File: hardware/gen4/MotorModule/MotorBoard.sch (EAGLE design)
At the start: 65 parts, among them IC1 XMEGA16A4A, IC2 3.3V REG, M1O1 TEST_PT, M1O2 TEST_PT, M1O3 TEST_PT

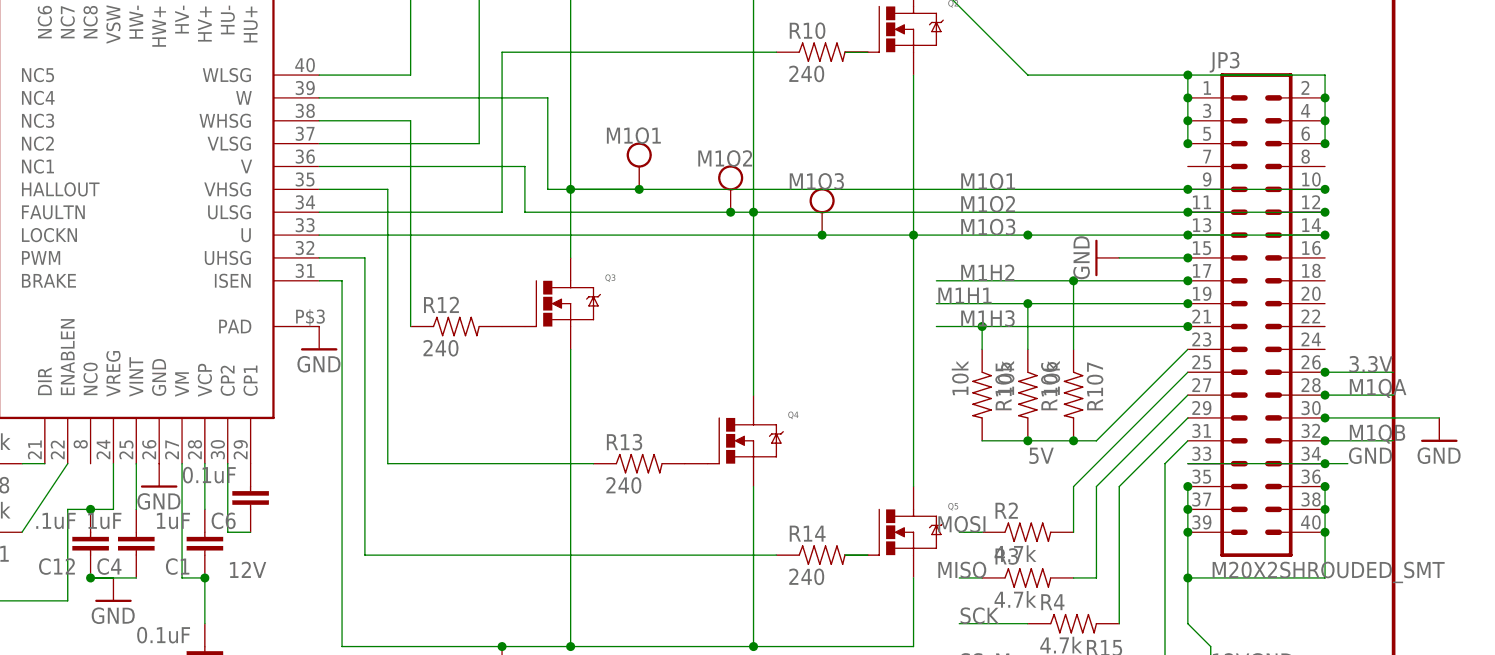
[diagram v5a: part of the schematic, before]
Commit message: extra motor pins
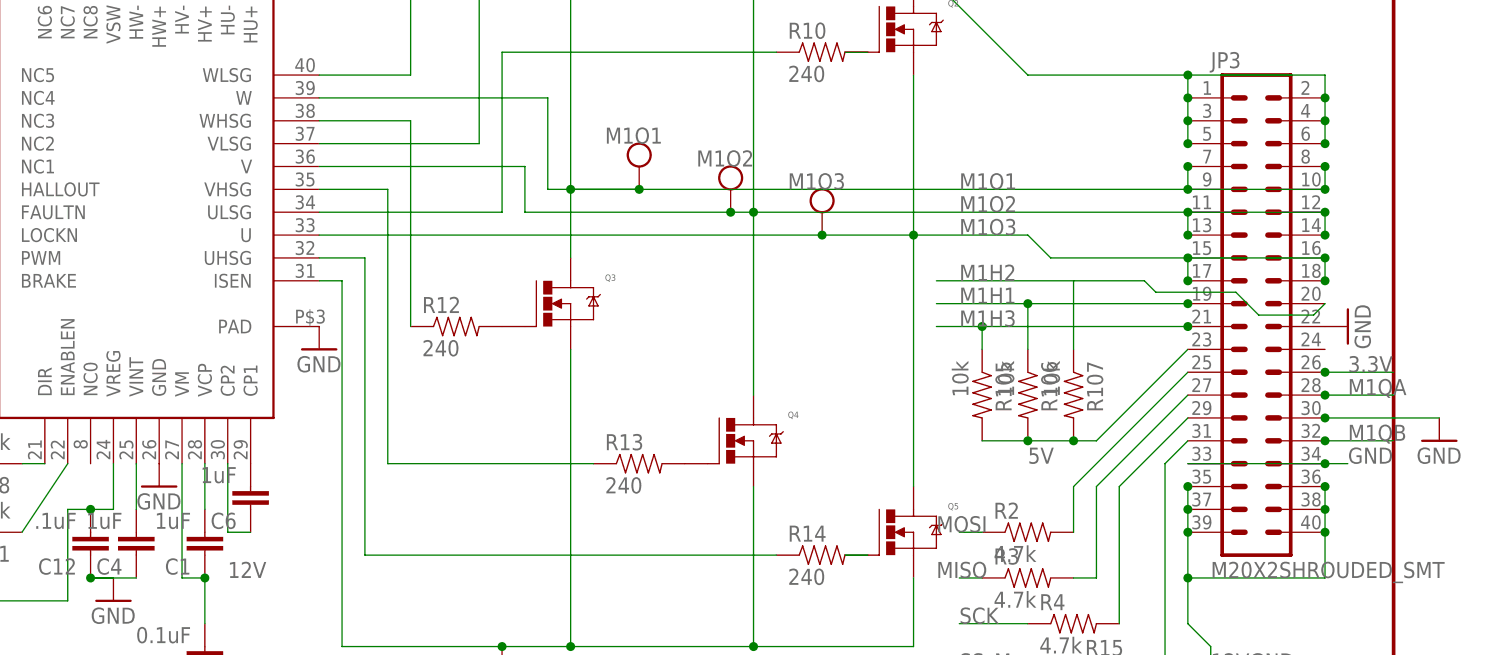
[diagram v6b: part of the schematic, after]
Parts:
- C6: value 0.1uF -> 1uF
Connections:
- net GND: now also JP3.22; no longer JP3.15
- net M1H2: now also JP3.20; no longer JP3.17
- net M1O1: now also JP3.7, JP3.8
- net M1O2: now also JP3.13, JP3.14
- net M1O3: now also JP3.15, JP3.16, JP3.17, JP3.18; no longer JP3.13, JP3.14
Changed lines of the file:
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@@
 <part name="R4" library="SparkFun-Passives" deviceset="RESISTOR" device="0805-RES" value="4.7k"/>
 <part name="C4" library="SparkFun-Passives" deviceset="CAP" device="0805" value="1uF"/>
-<part name="C6" library="SparkFun-Passives" deviceset="CAP" device="0805" value="0.1uF"/>
+<part name="C6" library="SparkFun-Passives" deviceset="CAP" device="0805" value="1uF"/>
 <part name="GND2" library="SparkFun-Aesthetics" deviceset="GND" device=""/>
 <part name="GND3" library="SparkFun-Aesthetics" deviceset="GND" device=""/>
@@
 <instance part="GND13" gate="1" x="127" y="93.98"/>
 <instance part="S2" gate="S" x="12.7" y="182.88"/>
-<instance part="GND10" gate="1" x="215.9" y="55.88" rot="R270"/>
+<instance part="GND10" gate="1" x="243.84" y="48.26" rot="R90"/>
 <instance part="GND14" gate="1" x="254" y="35.56"/>
 <instance part="U$1" gate="G$1" x="86.36" y="86.36" rot="R270"/>
@@
 </segment>
 <segment>
+<pinref part="JP3" gate="G$1" pin="22"/>
 <pinref part="GND10" gate="1" pin="GND"/>
-<pinref part="JP3" gate="G$1" pin="15"/>
-<wire x1="218.44" y1="55.88" x2="226.06" y2="55.88" width="0.1524" layer="91"/>
-<junction x="226.06" y="55.88"/>
 </segment>
 </net>
@@
 <junction x="226.06" y="63.5"/>
 <junction x="241.3" y="63.5"/>
+<pinref part="JP3" gate="G$1" pin="7"/>
+<wire x1="226.06" y1="63.5" x2="226.06" y2="66.04" width="0.1524" layer="91"/>
+<pinref part="JP3" gate="G$1" pin="8"/>
+<wire x1="241.3" y1="63.5" x2="241.3" y2="66.04" width="0.1524" layer="91"/>
+<junction x="226.06" y="66.04"/>
+<junction x="241.3" y="66.04"/>
 </segment>
 </net>
@@
 <junction x="241.3" y="60.96"/>
 <junction x="175.26" y="60.96"/>
+<pinref part="JP3" gate="G$1" pin="13"/>
+<wire x1="226.06" y1="60.96" x2="226.06" y2="58.42" width="0.1524" layer="91"/>
+<pinref part="JP3" gate="G$1" pin="14"/>
+<wire x1="241.3" y1="60.96" x2="241.3" y2="58.42" width="0.1524" layer="91"/>
+<junction x="226.06" y="58.42"/>
+<junction x="241.3" y="58.42"/>
 </segment>
 </net>
@@
 <junction x="185.42" y="58.42"/>
 <wire x1="208.28" y1="58.42" x2="195.58" y2="58.42" width="0.1524" layer="91"/>
-<wire x1="208.28" y1="58.42" x2="226.06" y2="58.42" width="0.1524" layer="91"/>
-<junction x="208.28" y="58.42"/>
 <pinref part="U$1" gate="G$1" pin="U"/>
-<pinref part="JP3" gate="G$1" pin="13"/>
-<pinref part="JP3" gate="G$1" pin="14"/>
-<wire x1="226.06" y1="58.42" x2="241.3" y2="58.42" width="0.1524" layer="91"/>
-<junction x="226.06" y="58.42"/>
-<junction x="241.3" y="58.42"/>
+<wire x1="208.28" y1="58.42" x2="210.82" y2="55.88" width="0.1524" layer="91"/>
+<pinref part="JP3" gate="G$1" pin="15"/>
+<wire x1="210.82" y1="55.88" x2="226.06" y2="55.88" width="0.1524" layer="91"/>
+<pinref part="JP3" gate="G$1" pin="17"/>
+<wire x1="226.06" y1="53.34" x2="226.06" y2="55.88" width="0.1524" layer="91"/>
+<pinref part="JP3" gate="G$1" pin="16"/>
+<wire x1="226.06" y1="55.88" x2="241.3" y2="55.88" width="0.1524" layer="91"/>
+<pinref part="JP3" gate="G$1" pin="18"/>
+<wire x1="241.3" y1="55.88" x2="241.3" y2="53.34" width="0.1524" layer="91"/>
+<junction x="226.06" y="53.34"/>
+<junction x="226.06" y="55.88"/>
+<junction x="241.3" y="55.88"/>
+<junction x="241.3" y="53.34"/>
 </segment>
 </net>
@@
 <wire x1="213.36" y1="53.34" x2="198.12" y2="53.34" width="0.1524" layer="91"/>
 <wire x1="213.36" y1="45.72" x2="213.36" y2="53.34" width="0.1524" layer="91"/>
-<pinref part="JP3" gate="G$1" pin="17"/>
-<wire x1="213.36" y1="53.34" x2="226.06" y2="53.34" width="0.1524" layer="91"/>
-<junction x="226.06" y="53.34"/>
-<junction x="213.36" y="53.34"/>
+<wire x1="213.36" y1="53.34" x2="221.234" y2="53.34" width="0.1524" layer="91"/>
+<wire x1="221.234" y1="53.34" x2="222.504" y2="52.07" width="0.1524" layer="91"/>
+<wire x1="222.504" y1="52.07" x2="231.394" y2="52.07" width="0.1524" layer="91"/>
+<wire x1="231.394" y1="52.07" x2="233.934" y2="49.53" width="0.1524" layer="91"/>
+<pinref part="JP3" gate="G$1" pin="20"/>
+<wire x1="233.934" y1="49.53" x2="240.03" y2="49.53" width="0.1524" layer="91"/>
+<wire x1="240.03" y1="49.53" x2="241.3" y2="50.8" width="0.1524" layer="91"/>
 </segment>
 <segment>
@@
 <net name="M1H1" class="0">
 <segment>
-<label x="198.12" y="50.8" size="1.778" layer="95"/>
+<label x="200.66" y="50.8" size="1.778" layer="95"/>
 <pinref part="R106" gate="G$1" pin="1"/>
 <wire x1="208.28" y1="50.8" x2="198.12" y2="50.8" width="0.1524" layer="91"/>

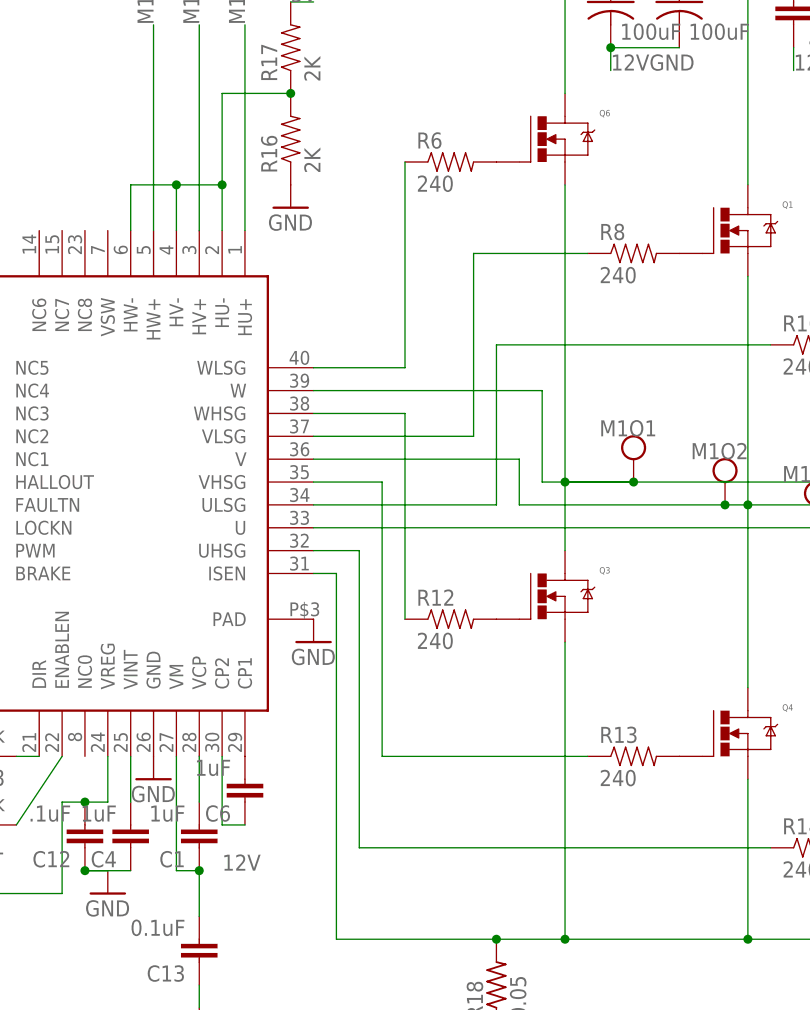
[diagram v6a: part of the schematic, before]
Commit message: highside lowside swtich
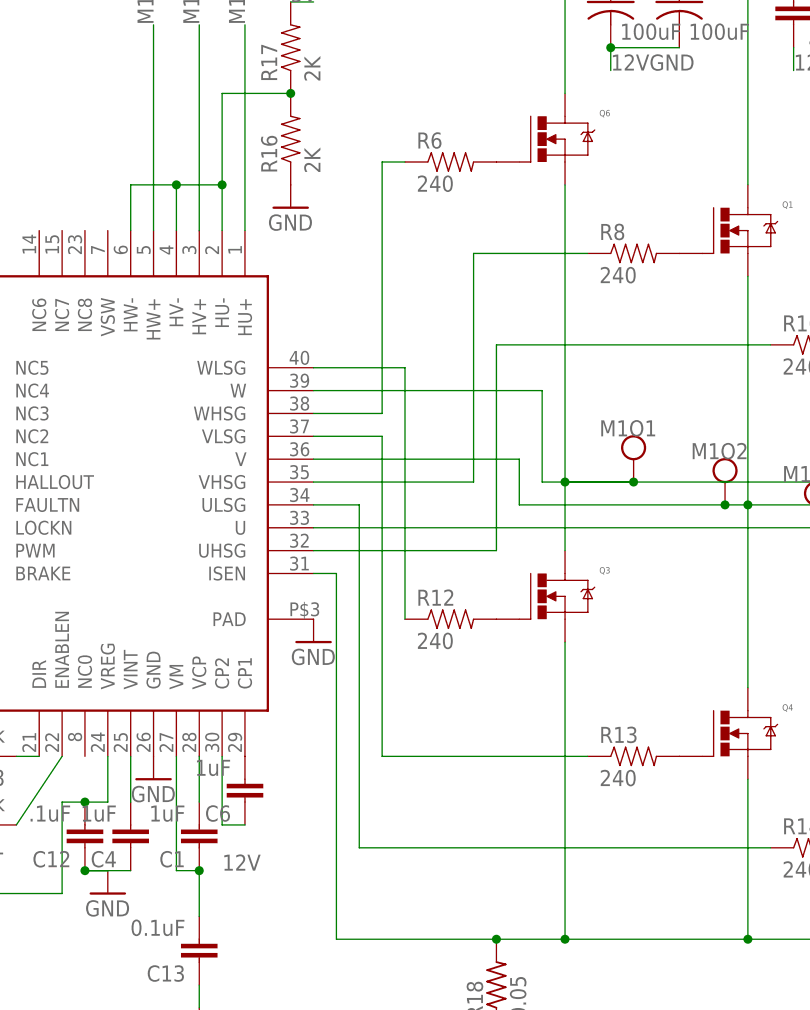
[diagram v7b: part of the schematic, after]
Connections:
- net N$16: now also U$1.WHSG; no longer U$1.WLSG
- net N$17: now also U$1.ULSG; no longer U$1.UHSG
- net N$18: now also U$1.VLSG; no longer U$1.VHSG
- net N$19: now also U$1.WLSG; no longer U$1.WHSG
- net N$20: now also U$1.VHSG; no longer U$1.VLSG
- net N$21: now also U$1.UHSG; no longer U$1.ULSG
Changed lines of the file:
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@@
 <segment>
 <pinref part="R6" gate="G$1" pin="1"/>
-<wire x1="139.7" y1="99.06" x2="139.7" y2="76.2" width="0.1524" layer="91"/>
-<wire x1="139.7" y1="76.2" x2="129.54" y2="76.2" width="0.1524" layer="91"/>
-<pinref part="U$1" gate="G$1" pin="WLSG"/>
+<wire x1="139.7" y1="99.06" x2="137.16" y2="99.06" width="0.1524" layer="91"/>
+<wire x1="137.16" y1="99.06" x2="137.16" y2="71.12" width="0.1524" layer="91"/>
+<pinref part="U$1" gate="G$1" pin="WHSG"/>
+<wire x1="137.16" y1="71.12" x2="129.54" y2="71.12" width="0.1524" layer="91"/>
 </segment>
 </net>
 <net name="N$17" class="0">
 <segment>
-<wire x1="129.54" y1="55.88" x2="134.62" y2="55.88" width="0.1524" layer="91"/>
-<wire x1="134.62" y1="55.88" x2="134.62" y2="22.86" width="0.1524" layer="91"/>
+<wire x1="134.62" y1="60.96" x2="134.62" y2="22.86" width="0.1524" layer="91"/>
 <pinref part="R14" gate="G$1" pin="1"/>
 <wire x1="134.62" y1="22.86" x2="180.34" y2="22.86" width="0.1524" layer="91"/>
-<pinref part="U$1" gate="G$1" pin="UHSG"/>
+<pinref part="U$1" gate="G$1" pin="ULSG"/>
+<wire x1="134.62" y1="60.96" x2="129.54" y2="60.96" width="0.1524" layer="91"/>
 </segment>
 </net>
 <net name="N$18" class="0">
 <segment>
-<wire x1="129.54" y1="63.5" x2="137.16" y2="63.5" width="0.1524" layer="91"/>
-<wire x1="137.16" y1="63.5" x2="137.16" y2="33.02" width="0.1524" layer="91"/>
+<wire x1="137.16" y1="68.58" x2="137.16" y2="33.02" width="0.1524" layer="91"/>
 <pinref part="R13" gate="G$1" pin="1"/>
 <wire x1="137.16" y1="33.02" x2="160.02" y2="33.02" width="0.1524" layer="91"/>
-<pinref part="U$1" gate="G$1" pin="VHSG"/>
+<pinref part="U$1" gate="G$1" pin="VLSG"/>
+<wire x1="137.16" y1="68.58" x2="129.54" y2="68.58" width="0.1524" layer="91"/>
 </segment>
 </net>
 <net name="N$19" class="0">
 <segment>
-<wire x1="129.54" y1="71.12" x2="139.7" y2="71.12" width="0.1524" layer="91"/>
-<wire x1="139.7" y1="71.12" x2="139.7" y2="48.26" width="0.1524" layer="91"/>
+<wire x1="139.7" y1="76.2" x2="139.7" y2="48.26" width="0.1524" layer="91"/>
 <pinref part="R12" gate="G$1" pin="1"/>
-<pinref part="U$1" gate="G$1" pin="WHSG"/>
+<pinref part="U$1" gate="G$1" pin="WLSG"/>
+<wire x1="139.7" y1="76.2" x2="129.54" y2="76.2" width="0.1524" layer="91"/>
 </segment>
 </net>
 <net name="N$20" class="0">
 <segment>
-<wire x1="129.54" y1="68.58" x2="147.32" y2="68.58" width="0.1524" layer="91"/>
-<wire x1="147.32" y1="68.58" x2="147.32" y2="88.9" width="0.1524" layer="91"/>
+<wire x1="147.32" y1="63.5" x2="147.32" y2="88.9" width="0.1524" layer="91"/>
 <pinref part="R8" gate="G$1" pin="1"/>
 <wire x1="147.32" y1="88.9" x2="160.02" y2="88.9" width="0.1524" layer="91"/>
-<pinref part="U$1" gate="G$1" pin="VLSG"/>
+<pinref part="U$1" gate="G$1" pin="VHSG"/>
+<wire x1="147.32" y1="63.5" x2="129.54" y2="63.5" width="0.1524" layer="91"/>
 </segment>
 </net>
@@
 <pinref part="R10" gate="G$1" pin="1"/>
 <wire x1="180.34" y1="78.74" x2="149.86" y2="78.74" width="0.1524" layer="91"/>
-<wire x1="149.86" y1="78.74" x2="149.86" y2="60.96" width="0.1524" layer="91"/>
-<wire x1="129.54" y1="60.96" x2="149.86" y2="60.96" width="0.1524" layer="91"/>
-<pinref part="U$1" gate="G$1" pin="ULSG"/>
+<wire x1="149.86" y1="78.74" x2="149.86" y2="55.88" width="0.1524" layer="91"/>
+<pinref part="U$1" gate="G$1" pin="UHSG"/>
+<wire x1="149.86" y1="55.88" x2="129.54" y2="55.88" width="0.1524" layer="91"/>
 </segment>
 </net>
